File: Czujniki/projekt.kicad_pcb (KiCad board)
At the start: 2 copper layers, 74.9 x 45.7 mm, 74 parts, among them P1 CONN_01X08, P2 CONN_01X06, P3 CONN_01X05, T1 Si2323DS, T2 FDV303N, T3 FDV303N, T4 Si2323DS, T5 Si2323DS, U1 MCP1700, U10 PCA9306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

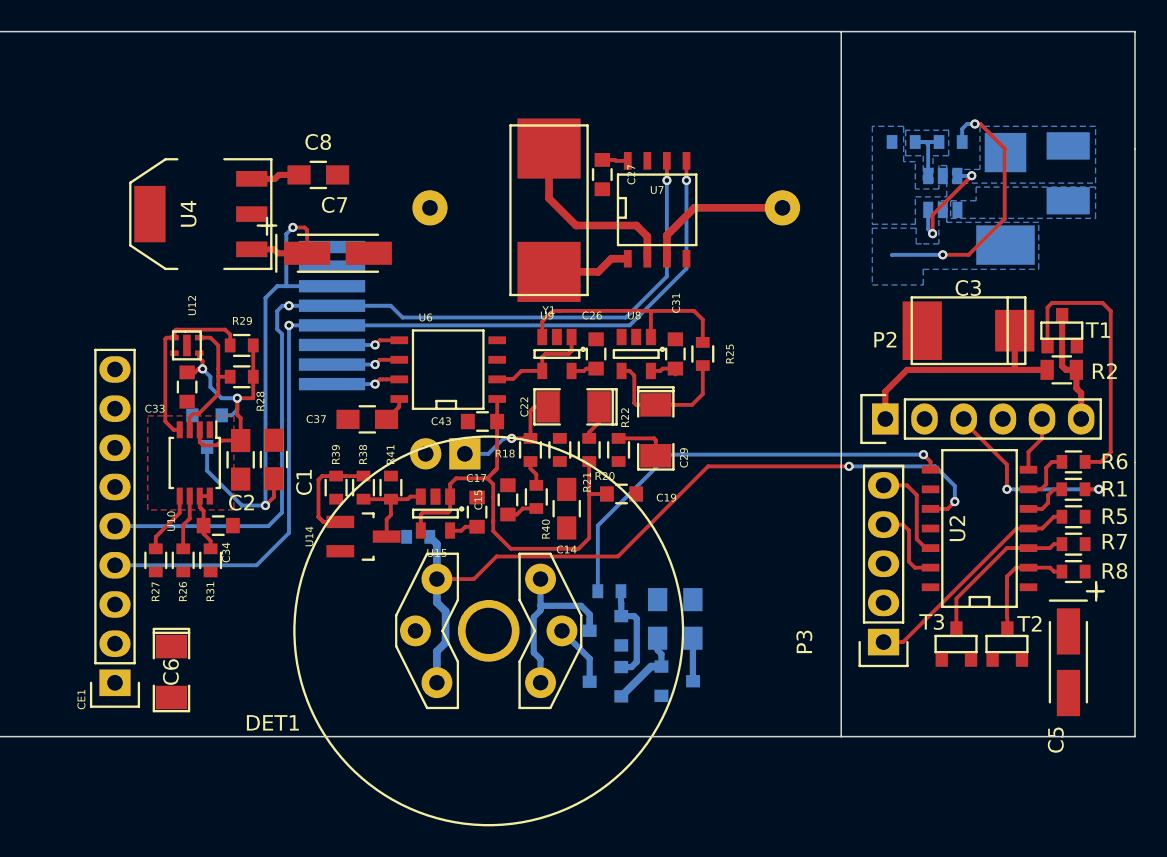
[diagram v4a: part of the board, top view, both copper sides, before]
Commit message: GND on sensor board for routing.
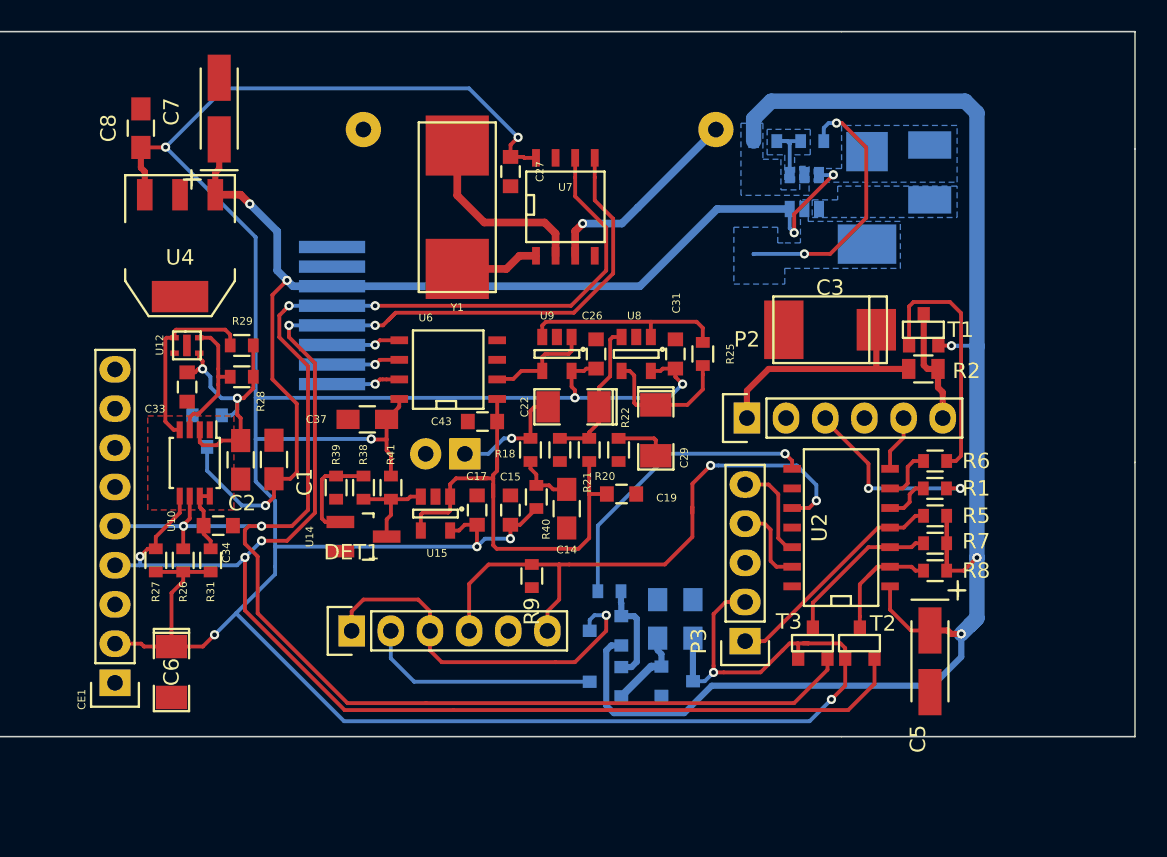
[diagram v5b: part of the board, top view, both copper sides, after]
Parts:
- DET1: footprint Footprinty:MQ-sensor -> Socket_Strips:Socket_Strip_Straight_1x06
- R9: moved to F.Cu
- moved C7 12.1 mm to (173.0, 60.2), turned to 90 degrees
- moved C8 11.9 mm to (167.9, 61.5), turned to 90 degrees
- moved T2 9.56 mm to (214.5, 94.9)
- moved T3 9.31 mm to (211.5, 94.9)
- moved C3 8.98 mm to (212.6, 74.6)
- moved C5 8.98 mm to (219.1, 96.1)
- moved L1 8.98 mm to (219.1, 64.4)
- moved R3 8.98 mm to (208.4, 62.3)
- moved R4 8.98 mm to (211.5, 62.3)
- moved C4 8.98 mm to (215.0, 66.0)
- moved P2 8.98 mm to (207.2, 80.3)
- moved P3 8.98 mm to (207.1, 94.8)
- moved R1 8.98 mm to (219.4, 84.9)
- moved R2 8.98 mm to (218.7, 77.1)
- moved R5 8.98 mm to (219.4, 86.6)
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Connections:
- P1 pad 7: VDD -> (no net)
- U2 pad 11: SENSAN2 -> (no net)
- U2 pad 9: DRV2 -> (no net)
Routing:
- net VDD: track 16.9 -> 222.8 mm, vias 0 -> 10
- net +5V: track 0.00 -> 101.1 mm, vias 0 -> 3
- net SDA: track 64.0 -> 113.4 mm, vias 2 -> 5
- net SCL: track 62.3 -> 108.4 mm, vias 2 -> 4
- net MAIN_VOL: track 43.9 -> 77.7 mm, vias 4 -> 5
- net Net-(DET1-PadA): track 12.4 -> 25.0 mm, vias 0 -> 1
- net Net-(DET1-PadH1): track 4.04 -> 15.3 mm
- net SENSAN1: track 50.0 -> 39.1 mm
- net DRV1: track 28.4 -> 19.5 mm
- net Net-(C22-Pad1): track 2.31 -> 9.68 mm
- net ADCREF: track 30.0 -> 32.2 mm
- net Net-(C14-Pad1): track 1.71 -> 3.78 mm
- net Net-(BT1-Pad1): track 15.5 -> 13.5 mm, vias 0 -> 1
- net Net-(R25-Pad1): track 15.2 -> 13.4 mm
- net Net-(R6-Pad2): track 18.0 -> 16.7 mm
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
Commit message: Ground plane and license.
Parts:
- moved R9 0.70 mm to (193.3, 91.2)
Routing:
- net GND: track 17.3 -> 333.1 mm, vias 2 -> 72
- net (no net): track 0.00 -> 8.87 mm, vias 0 -> 3
- net VDD: track 222.8 -> 226.3 mm
- net SCL: track 108.4 -> 110.4 mm
- net SDA: track 113.4 -> 115.0 mm
- net RESETSIG: track 14.9 -> 16.2 mm
- net SENSAN1: track 39.1 -> 38.4 mm
- net INP: track 7.05 -> 6.49 mm
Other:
- board text added: "EkoPuszka"
- board text added: "SK 2015"
- board text added: "Sławomir Kozok"

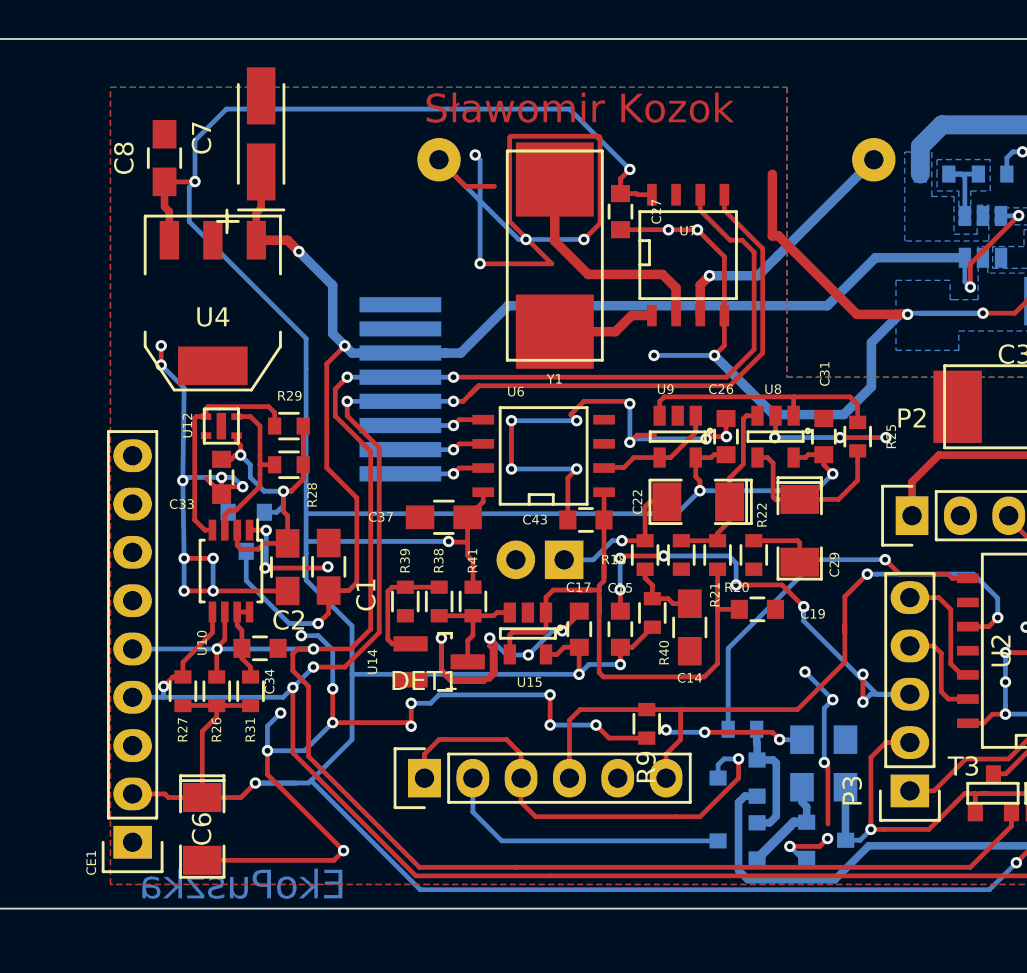
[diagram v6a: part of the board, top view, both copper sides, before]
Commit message: Adding license files. PCB ready for fixes.
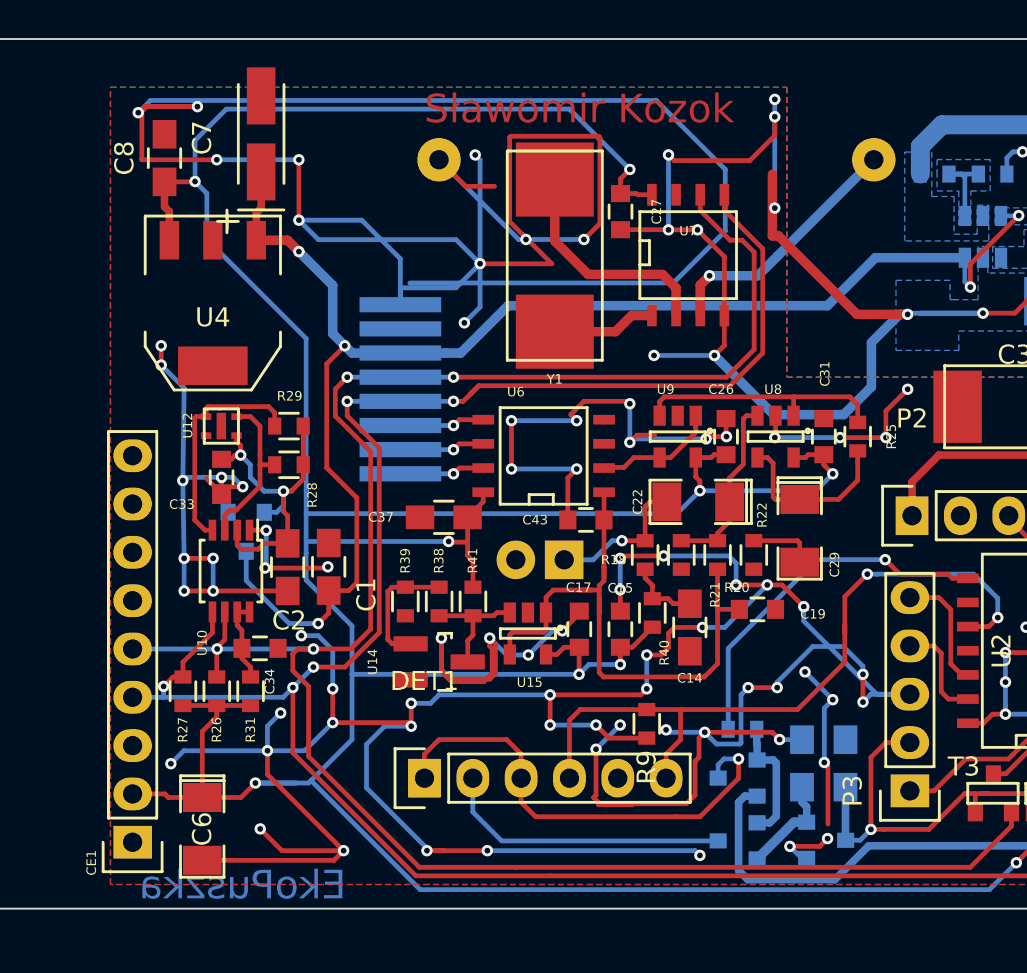
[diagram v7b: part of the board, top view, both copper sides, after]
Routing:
- net GND: track 333.1 -> 533.0 mm, vias 72 -> 96

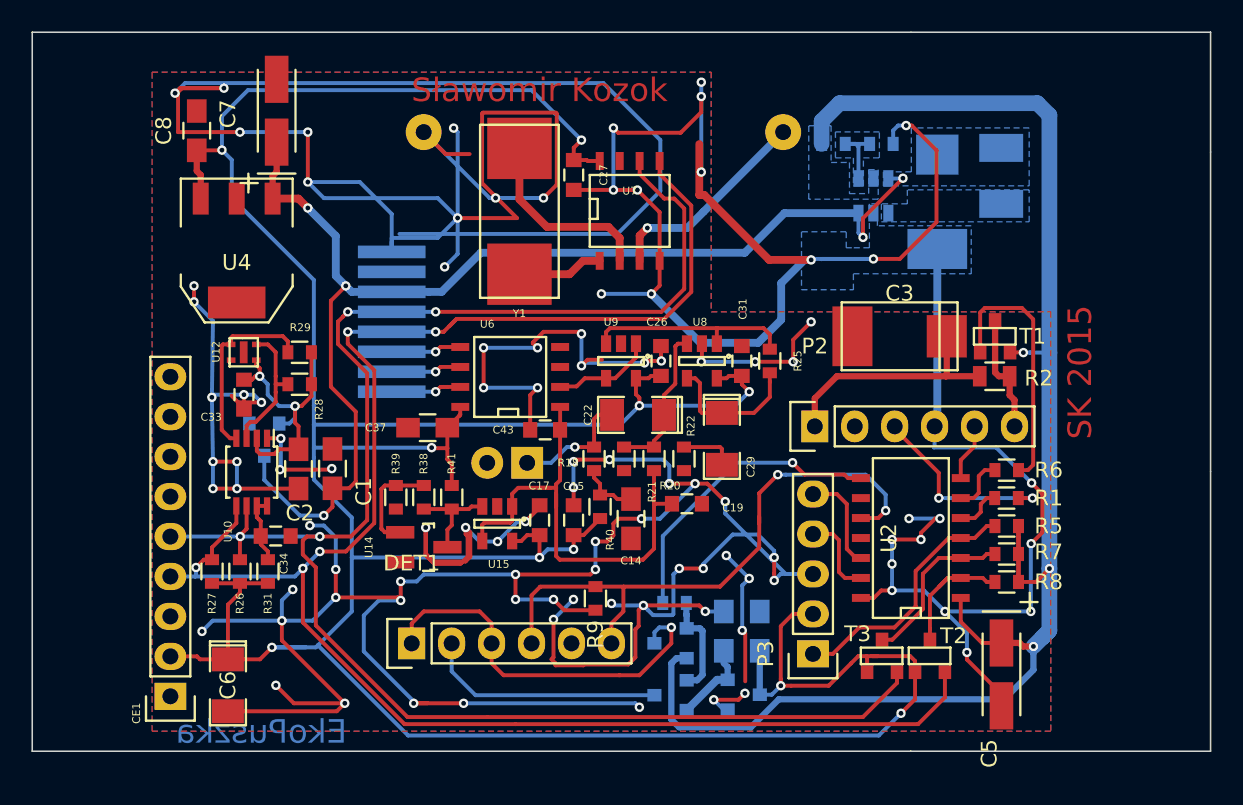
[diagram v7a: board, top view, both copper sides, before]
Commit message: Change board sizes.
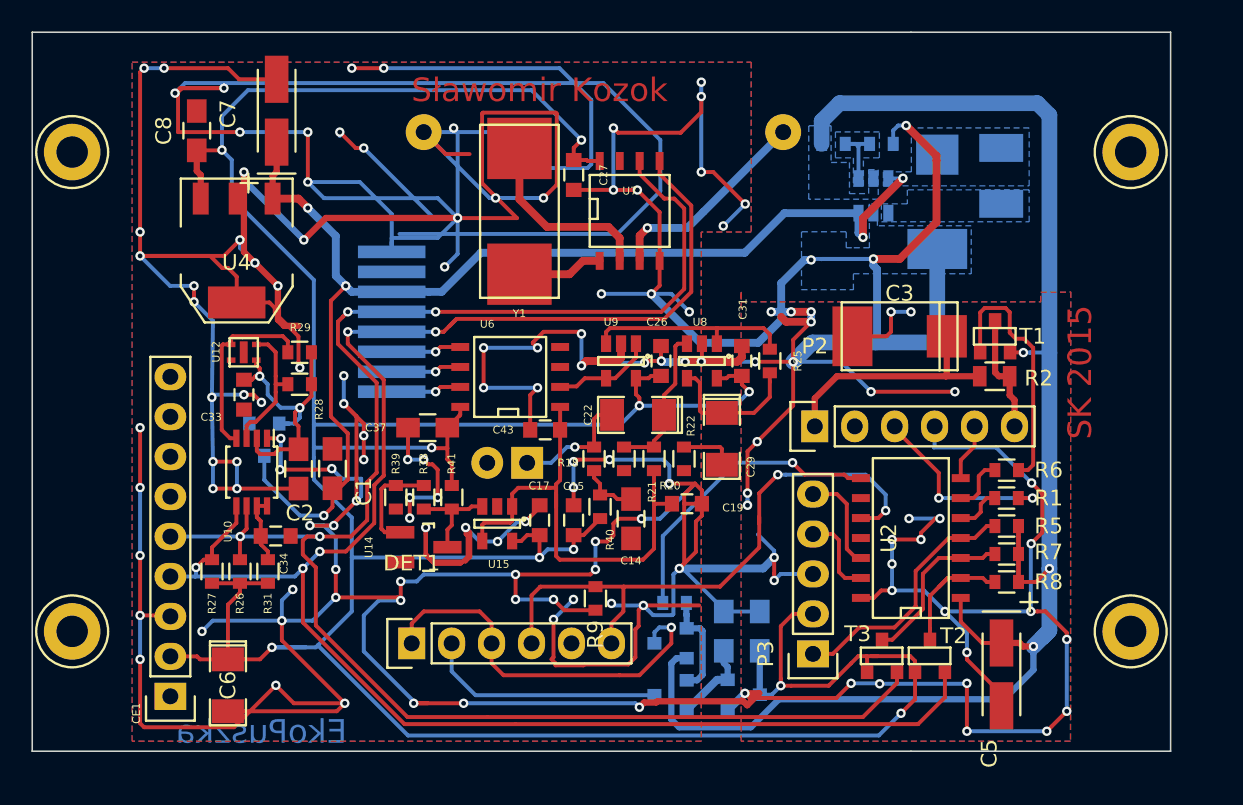
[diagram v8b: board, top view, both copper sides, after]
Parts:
- added REF**: 1pin, Connect:1pin, F.Cu at (160.0, 93.3)
- added REF**: 1pin, Connect:1pin, F.Cu at (160.0, 62.9)
- added REF**: 1pin, Connect:1pin, F.Cu at (227.3, 62.9)
- added REF**: 1pin, Connect:1pin, F.Cu at (227.3, 93.3)
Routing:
- net GND: track 533.0 -> 806.8 mm, vias 96 -> 142
- net (no net): track 8.87 -> 0.00 mm, vias 3 -> 0
- net +1V8: track 18.1 -> 19.1 mm
- net MAIN_VOL: track 77.7 -> 77.0 mm
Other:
- board size 74.9 x 45.7 mm -> 72.4 x 45.7 mm
